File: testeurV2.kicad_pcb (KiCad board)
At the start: 2 copper layers, 32 parts, among them J1 I2C_a, J10 CAN, J2 I2C_b, J3 S1, J4 S2, J5 S3, J6 S4, J7 S5, J8 22-03-5035, J9 22-03-5035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

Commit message: testeurV2 R0.1
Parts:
- added REF**: mountingHole_2mm, myFootprints:mountingHole_2mm, F.Cu at (99.0, 41.0)
- added REF**: mountingHole_2mm, myFootprints:mountingHole_2mm, F.Cu at (198.0, 41.0)
- added REF**: mountingHole_2mm, myFootprints:mountingHole_2mm, F.Cu at (198.0, 100.0)
- added REF**: mountingHole_2mm, myFootprints:mountingHole_2mm, F.Cu at (99.0, 100.0)
- C4: moved to B.Cu
- moved P1 43.7 mm to (189.9, 45.1)
- moved R5 35.0 mm to (198.1, 51.0), turned to 90 degrees
- moved R4 34.0 mm to (196.2, 51.0), turned to 270 degrees
- moved C4 26.2 mm to (167.6, 66.7), turned to 270 degrees
- moved D1 24.0 mm to (127.0, 99.2), turned to 90 degrees
- moved U1 23.8 mm to (189.9, 54.0), turned to 180 degrees
- moved C1 23.6 mm to (110.3, 61.0)
- moved R2 20.8 mm to (127.0, 93.5), turned to 90 degrees
- moved R3 20.1 mm to (132.6, 94.0), turned to 180 degrees
- moved RV1 18.1 mm to (113.2, 68.7), turned to 90 degrees
- moved U2 16.6 mm to (110.5, 57.1)
- moved D2 15.9 mm to (134.6, 99.2), turned to 90 degrees
- moved SW1 11.7 mm to (187.2, 77.6), turned to 90 degrees
- moved R1 11.1 mm to (125.1, 49.0), turned to 90 degrees
- moved C6 7.95 mm to (189.2, 68.1), turned to 90 degrees
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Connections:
- U4 pad 1: +5V -> GND
- U4 pad 11: Net-(DS1-Pad4) -> Net-(DS1-Pad6)
- U4 pad 2: +5V -> GND
- U4 pad 3: +5V -> GND
- U4 pad 4: Net-(DS1-Pad14) -> Net-(DS1-Pad13)
- U4 pad 5: Net-(DS1-Pad13) -> Net-(DS1-Pad14)
- U4 pad 9: Net-(DS1-Pad6) -> Net-(DS1-Pad4)
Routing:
- net GND: track 0.00 -> 522.3 mm, vias 0 -> 3
- net +5V: track 0.00 -> 223.1 mm, vias 0 -> 3
- net /DYNAMIXEL: track 0.00 -> 127.3 mm, vias 0 -> 1
- net /BAT_MEAS: track 0.00 -> 126.9 mm, vias 0 -> 1
- net /I2C1_SDA: track 0.00 -> 117.3 mm, vias 0 -> 1
- net /I2C1_SCL: track 0.00 -> 108.8 mm, vias 0 -> 1
- net /SERVO4: track 0.00 -> 68.5 mm, vias 0 -> 1
- net /SERVO1: track 0.00 -> 66.1 mm, vias 0 -> 1
- net /SERVO5: track 0.00 -> 65.7 mm, vias 0 -> 1
- net /ENC_B: track 0.00 -> 65.2 mm
- net /ENC_A: track 0.00 -> 64.1 mm
- net /RET_BTN: track 0.00 -> 63.7 mm, vias 0 -> 1
- net /CAN_RX: track 0.00 -> 59.8 mm, vias 0 -> 1
- net /OK_BTN: track 0.00 -> 54.8 mm, vias 0 -> 1
- net Net-(DS1-Pad4): track 0.00 -> 54.0 mm
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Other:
- board outline added: 105 x 65 mm
- net class Default: clearance 0.2 -> 0.4; trace_width 0.25 -> 0.8; via_dia 0.8 -> 1.9; via_drill 0.4 -> 0.8
- rule trace_clearance: 0.2 -> 0.4
- board text added: "2019"
- board text added: "CAN"
- board text added: "DYN"
- board text added: "Fab@ENAC"
- board text added: "I2C"
- board text added: "S1"
- board text added: "S2"
- board text added: "S3"
- board text added: "S4"
- board text added: "S5"
- board text added: "Testeur"
- board text added: "↵"

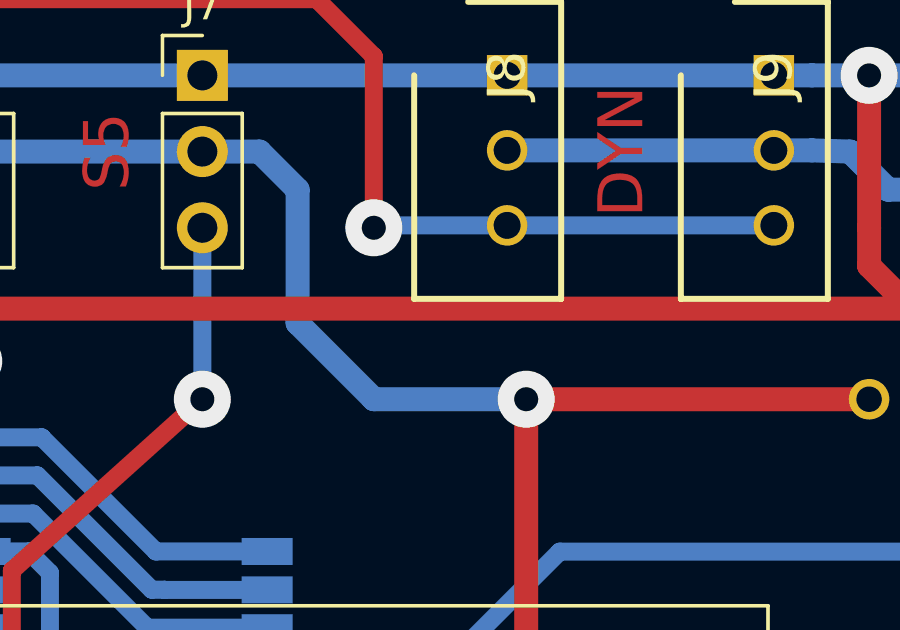
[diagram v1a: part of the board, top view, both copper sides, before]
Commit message: Adds pullup for dynamixels.
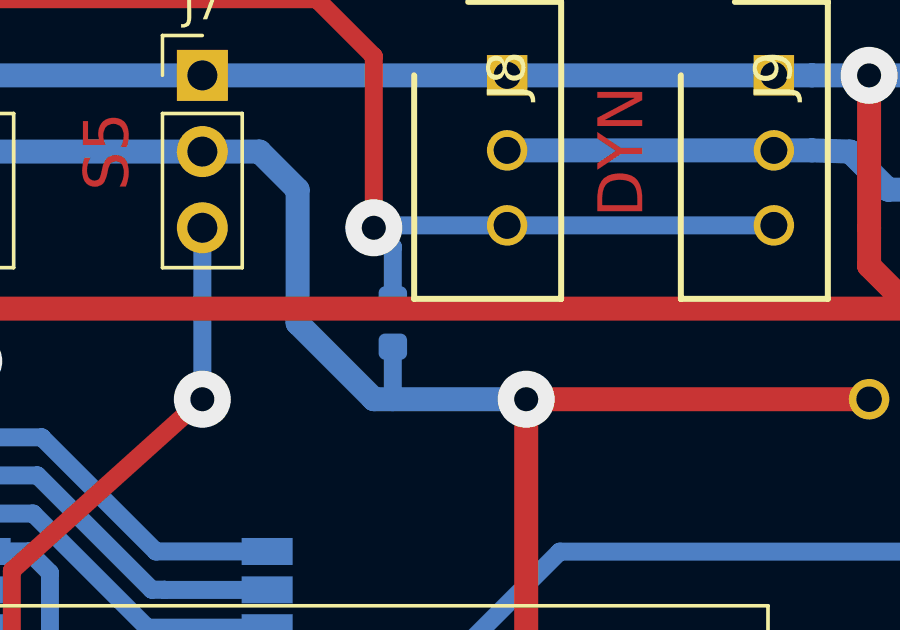
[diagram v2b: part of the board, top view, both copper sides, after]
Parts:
- added R6: 1k, Resistor_SMD:R_0603_1608Metric, B.Cu at (168.9, 51.4)
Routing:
- net /DYNAMIXEL: track 127.3 -> 129.9 mm
- net +5V: track 223.1 -> 224.9 mm
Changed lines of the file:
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@@
     (thickness 1.6)
     (drawings 16)
-    (tracks 429)
+    (tracks 433)
     (zones 0)
-    (modules 36)
+    (modules 37)
     (nets 33)
   )
@@
     )
     (pad 1 thru_hole circle (at 0 0) (size 2 2) (drill 0.5) (layers *.Cu *.Mask))
+  )
+  (module Resistor_SMD:R_0603_1608Metric (layer B.Cu)
+    (at 168.91 51.435 270)
+    (descr "Resistor SMD 0603 (1608 Metric), square (rectangular) end terminal, IPC_7351 nominal, (Body size source: http://www.tortai-tech.com/upload/download/2011102023233369053.pdf), generated with kicad-footprint-generator")
+    (tags resistor)
+    (attr smd)
+    (fp_text reference R6 (at 0 1.43 270) (layer B.SilkS)
+      (effects (font (size 1 1) (thickness 0.15)) (justify mirror))
+    )
+    (fp_text value 1k (at 0 -1.43 270) (layer B.Fab)
+      (effects (font (size 1 1) (thickness 0.15)) (justify mirror))
+    )
+    (fp_line (start -0.8 -0.4) (end -0.8 0.4) (layer B.Fab) (width 0.1))
+    (fp_line (start -0.8 0.4) (end 0.8 0.4) (layer B.Fab) (width 0.1))
+    (fp_line (start 0.8 0.4) (end 0.8 -0.4) (layer B.Fab) (width 0.1))
+    (fp_line (start 0.8 -0.4) (end -0.8 -0.4) (layer B.Fab) (width 0.1))
+    (fp_line (start -0.162779 0.51) (end 0.162779 0.51) (layer B.SilkS) (width 0.12))
+    (fp_line (start -0.162779 -0.51) (end 0.162779 -0.51) (layer B.SilkS) (width 0.12))
+    (fp_line (start -1.48 -0.73) (end -1.48 0.73) (layer B.CrtYd) (width 0.05))
+    (fp_line (start -1.48 0.73) (end 1.48 0.73) (layer B.CrtYd) (width 0.05))
+    (fp_line (start 1.48 0.73) (end 1.48 -0.73) (layer B.CrtYd) (width 0.05))
+    (fp_line (start 1.48 -0.73) (end -1.48 -0.73) (layer B.CrtYd) (width 0.05))
+    (fp_text user %R (at 0 0 270) (layer B.Fab)
+      (effects (font (size 0.4 0.4) (thickness 0.06)) (justify mirror))
+    )
+    (pad 1 smd roundrect (at -0.7875 0 270) (size 0.875 0.95) (layers B.Cu B.Paste B.Mask) (roundrect_rratio 0.25)
+      (net 24 /DYNAMIXEL))
+    (pad 2 smd roundrect (at 0.7875 0 270) (size 0.875 0.95) (layers B.Cu B.Paste B.Mask) (roundrect_rratio 0.25)
+      (net 2 +5V))
+    (model ${KISYS3DMOD}/Resistor_SMD.3dshapes/R_0603_1608Metric.wrl
+      (at (xyz 0 0 0))
+      (scale (xyz 1 1 1))
+      (rotate (xyz 0 0 0))
+    )
   )
   (gr_text 2019 (at 173.99 80.645) (layer B.Cu)
@@
   (segment (start 165.735 46.99) (end 164.465 45.72) (width 0.8) (layer B.Cu) (net 2))
   (segment (start 165.735 51.435) (end 165.735 46.99) (width 0.8) (layer B.Cu) (net 2))
-  (segment (start 173.355 53.975) (end 168.275 53.975) (width 0.8) (layer B.Cu) (net 2))
   (segment (start 168.275 53.975) (end 165.735 51.435) (width 0.8) (layer B.Cu) (net 2))
   (via (at 116.84 85.09) (size 1.9) (drill 0.8) (layers F.Cu B.Cu) (net 2))
@@
   (segment (start 150.074937 71.969937) (end 157.265063 71.969937) (width 0.8) (layer B.Cu) (net 2))
   (segment (start 173.355 53.975) (end 184.785 53.975) (width 0.8) (layer F.Cu) (net 2))
+  (segment (start 168.91 52.2225) (end 168.91 53.975) (width 0.6) (layer B.Cu) (net 2))
+  (segment (start 173.355 53.975) (end 168.91 53.975) (width 0.8) (layer B.Cu) (net 2))
+  (segment (start 168.91 53.975) (end 168.275 53.975) (width 0.8) (layer B.Cu) (net 2))
   (segment (start 187.162248 80.807752) (end 187.162248 77.582014) (width 0.6) (layer F.Cu) (net 3))
   (segment (start 136.525 85.725) (end 182.245 85.725) (width 0.6) (layer F.Cu) (net 3))
@@
   (segment (start 99.695 71.12) (end 102.235 73.66) (width 0.6) (layer F.Cu) (net 24))
   (segment (start 103.505 40.64) (end 99.695 44.45) (width 0.6) (layer F.Cu) (net 24))
+  (segment (start 168.91 48.895) (end 168.275 48.26) (width 0.6) (layer B.Cu) (net 24))
+  (segment (start 168.91 50.6475) (end 168.91 48.895) (width 0.6) (layer B.Cu) (net 24))
   (segment (start 194.31 46.99) (end 185.42 46.99) (width 0.8) (layer B.Cu) (net 25))
   (via (at 194.31 46.99) (size 1.9) (drill 0.8) (layers F.Cu B.Cu) (net 25))

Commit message: Adds MAX6818 to debounce buttons. Adds missing pullup on dynamixel UART.
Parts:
- removed C3, C5, C6: 100n, Capacitor_SMD:C_0603_1608Metric
- added U5: MAX6818, Package_SO:SSOP-20_5.3x7.2mm_P0.65mm, B.Cu at (171.4, 80.0)
- moved C2 16.2 mm to (171.0, 73.7)
- moved SW1 16.0 mm to (191.8, 62.2), turned to 270 degrees
- moved SW2 7.10 mm to (191.8, 86.4), turned to 270 degrees
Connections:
- C2 pad 2: /ENC_A -> +5V
- SW1 pad A: /ENC_A -> Net-(SW1-PadA)
- SW1 pad B: /ENC_B -> Net-(SW1-PadB)
- SW1 pad S1: /OK_BTN -> Net-(SW1-PadS1)
- SW2 pad 1: /RET_BTN -> GND
- SW2 pad 2: GND -> Net-(SW2-Pad2)
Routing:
- net /RET_BTN: track 63.7 -> 30.1 mm
- net Net-(SW1-PadA): track 0.00 -> 33.4 mm
- net /OK_BTN: track 54.8 -> 26.2 mm
- net GND: track 522.3 -> 549.8 mm
- net /ENC_B: track 65.2 -> 39.5 mm, vias 0 -> 1
- net Net-(SW1-PadB): track 0.00 -> 23.6 mm
- net /ENC_A: track 64.1 -> 40.8 mm, vias 0 -> 1
- net Net-(SW2-Pad2): track 0.00 -> 21.5 mm
- net Net-(SW1-PadS1): track 0.00 -> 13.0 mm
- net +5V: track 224.9 -> 236.4 mm
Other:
- net class Default: clearance 0.4 -> 0.2
- rule trace_clearance: 0.4 -> 0.2
- board text added: "Testeur V2.2"
- board text removed: "Testeur"
